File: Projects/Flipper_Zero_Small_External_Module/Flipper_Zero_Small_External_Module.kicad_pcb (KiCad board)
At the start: 2 copper layers, 65.3 x 15.7 mm, 2 parts, among them J1 Flipper_Zero

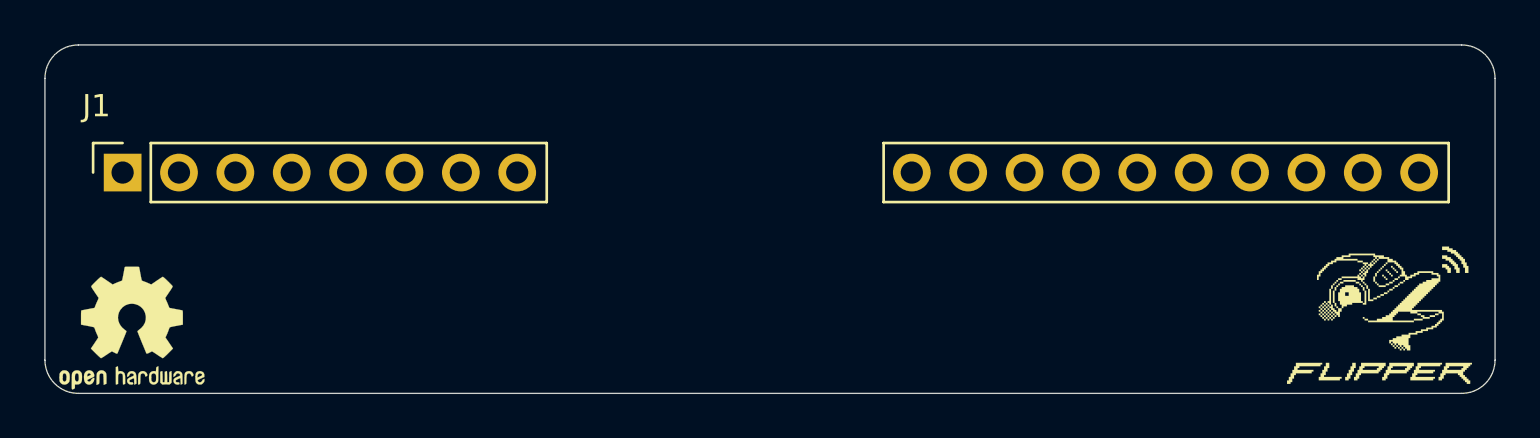
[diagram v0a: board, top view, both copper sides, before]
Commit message: Update to KiCAD 10
Signed-off-by: Ilias Daradimos <judgedrid@gmail.com>
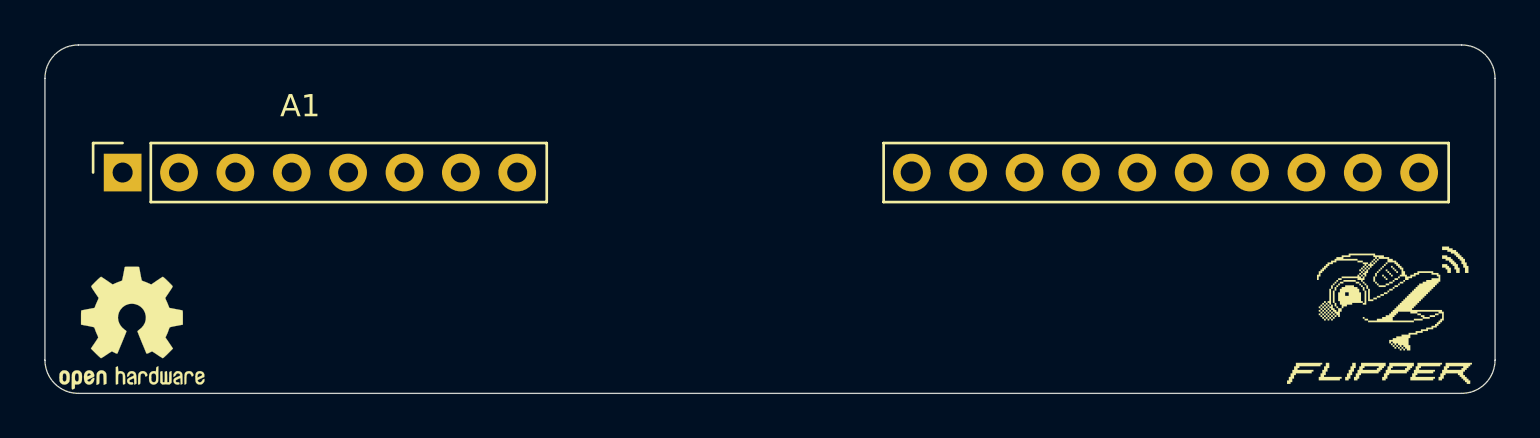
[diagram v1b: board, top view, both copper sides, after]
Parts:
- renumbered J1 to A1
